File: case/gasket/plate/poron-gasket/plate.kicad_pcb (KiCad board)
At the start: 2 copper layers, 152.4 x 66.2 mm, 0 parts

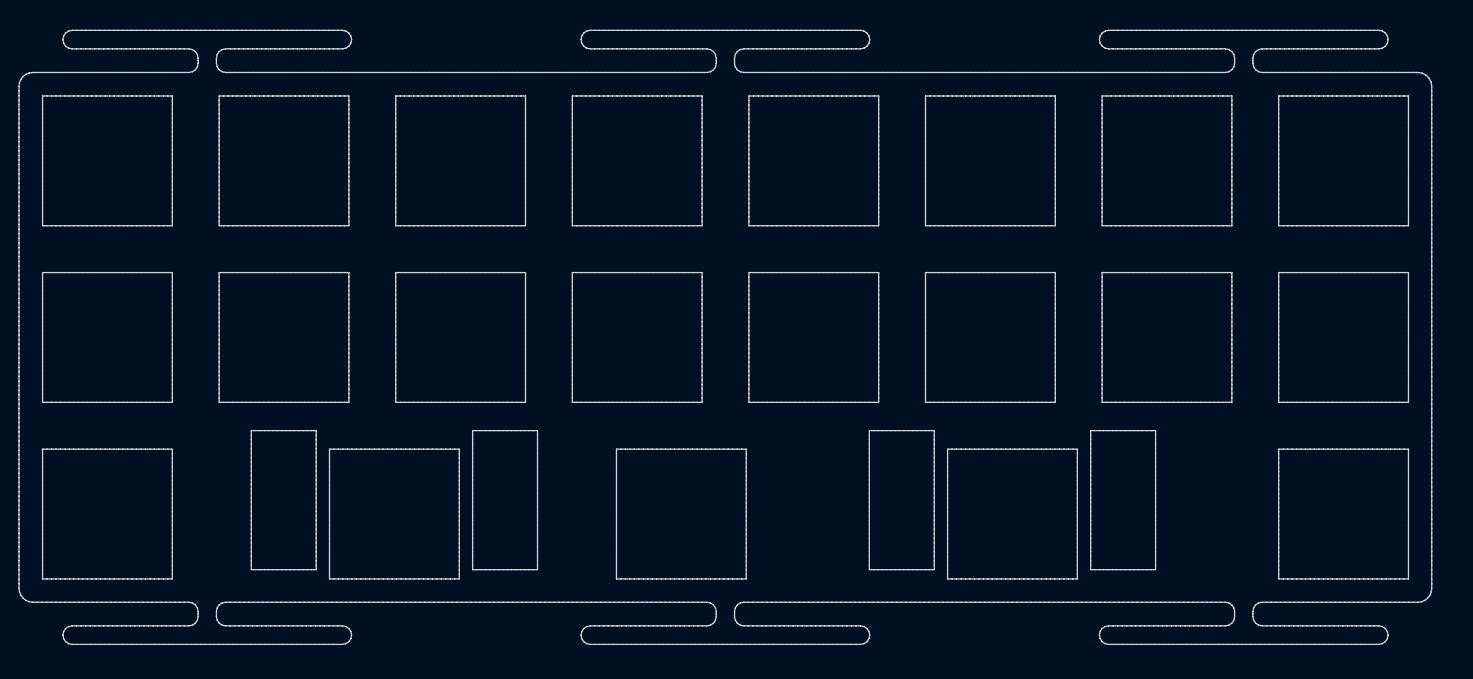
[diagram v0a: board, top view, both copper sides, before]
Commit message: add gasket mount plate for poron
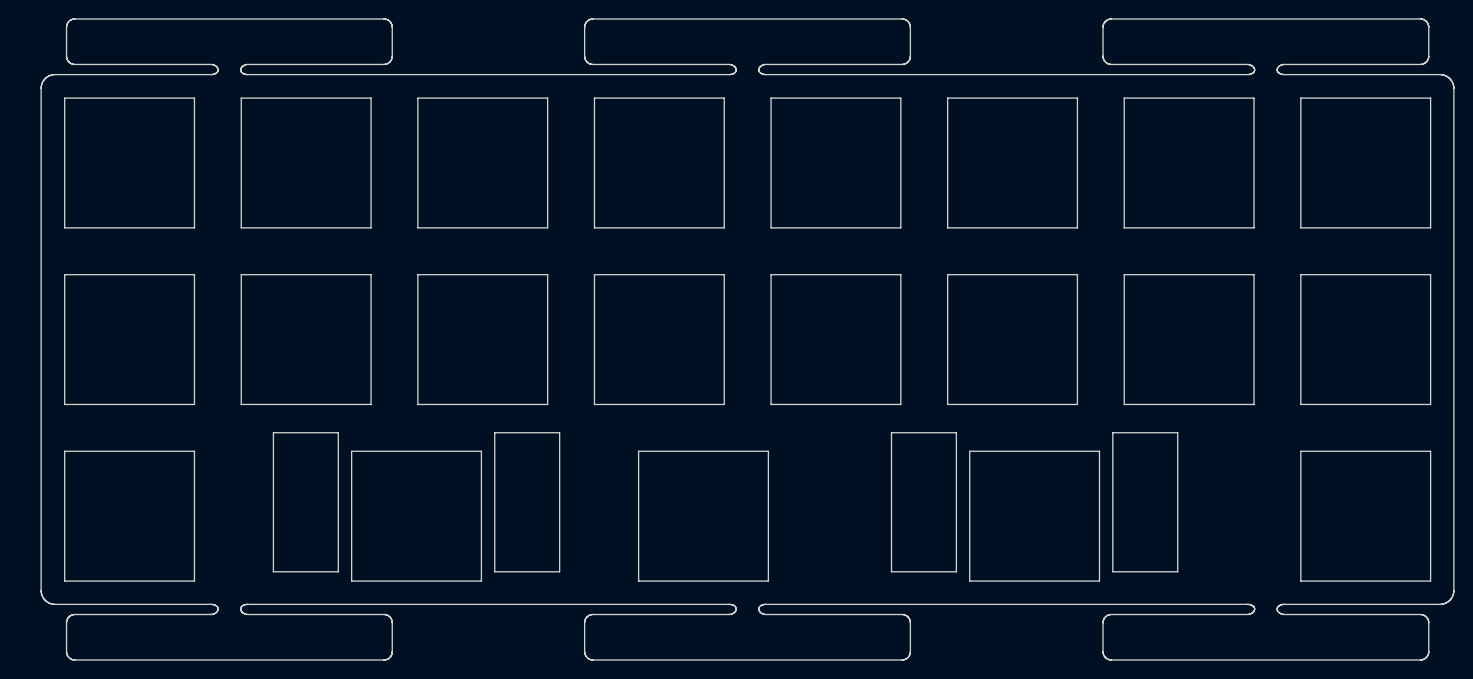
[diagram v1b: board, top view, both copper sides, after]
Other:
- board size 152.4 x 66.2 mm -> 152.4 x 69.1 mm
